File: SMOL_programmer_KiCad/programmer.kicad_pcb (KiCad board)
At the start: 2 copper layers, 9.7 x 24.9 mm, 13 parts, among them J1 Conn_02x03_Odd_Even, J2 Conn_01x05, J3 Conn_01x05

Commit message: Updated gerbs, added folder for AVR programs
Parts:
- removed REF** (x6): Mounting_Hole, samsam_footprints:Mounting_Hole
- moved R1 0.25 mm to (97.8, 111.1)
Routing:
- net /att_reset: track 7.16 -> 9.04 mm
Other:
- board size 9.7 x 24.9 mm -> 9.7 x 18.8 mm

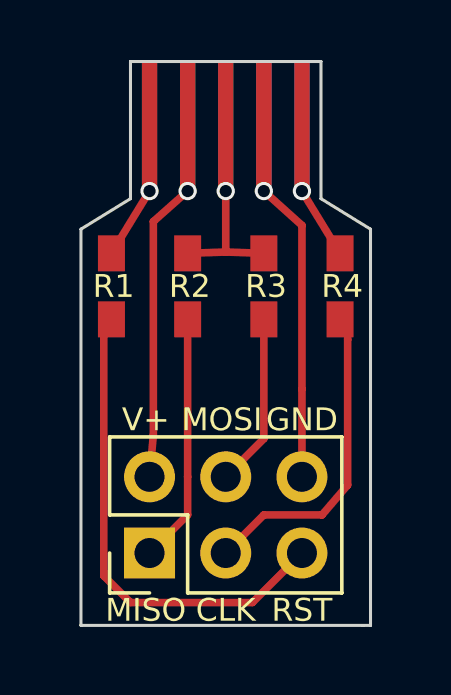
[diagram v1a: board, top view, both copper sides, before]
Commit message: re-jigging the form factor of circuit revision 6
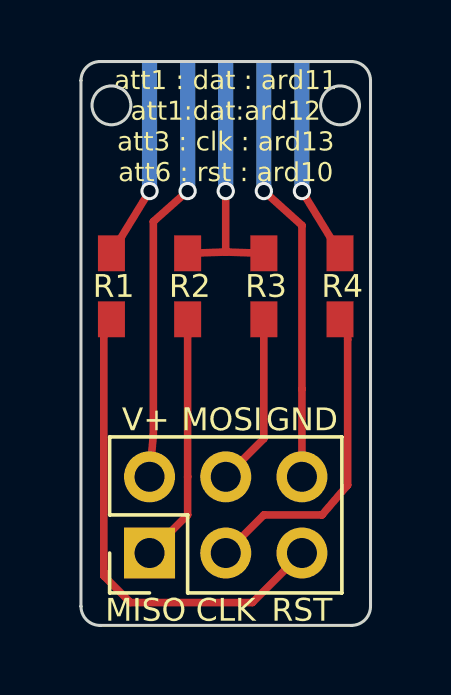
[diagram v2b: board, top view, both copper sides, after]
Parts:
- removed J2: Conn_01x05, SMOL_footprints:edgeconn
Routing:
- net /att_reset: track 9.04 -> 4.08 mm
- net GNDREF: track 15.0 -> 11.7 mm
- net /pwr: track 15.0 -> 11.7 mm
- net /att_data: track 9.53 -> 6.22 mm
- net /att_clk: track 7.39 -> 4.08 mm
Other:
- outline, holes or cut-outs redrawn
- board text added: "att1 : dat : ard11 att1:dat:ard12 att3 : clk : ard13 att6 : rst : ard10"
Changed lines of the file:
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@@
-(kicad_pcb (version 20171130) (host pcbnew "(5.0.1)-3")
+(kicad_pcb (version 20171130) (host pcbnew "(5.0.2)-1")
   (general
     (thickness 1.6)
-    (drawings 16)
-    (tracks 48)
+    (drawings 18)
+    (tracks 38)
     (zones 0)
-    (modules 7)
+    (modules 6)
     (nets 10)
   )
@@
     (36 B.SilkS user)
     (37 F.SilkS user)
-    (38 B.Mask user)
+    (38 B.Mask user hide)
     (39 F.Mask user hide)
-    (40 Dwgs.User user)
-    (41 Cmts.User user)
+    (40 Dwgs.User user hide)
+    (41 Cmts.User user hide)
     (44 Edge.Cuts user)
     (45 Margin user)
@@
     (solder_mask_min_width 0.25)
     (aux_axis_origin 0 0)
-    (visible_elements 7FEFFF7F)
+    (visible_elements 7FFFFF7F)
     (pcbplotparams
       (layerselection 0x010f0_ffffffff)
@@
     )
   )
-  (module SMOL_footprints:edgeconn (layer F.Cu)
-    (at 99.06 106.299 90)
-    (descr "Through hole straight pin header, 1x06, 2.00mm pitch, single row")
-    (tags "Through hole pin header THT 1x06 2.00mm single row")
-    (fp_text reference J2 (at 0 -2.06 90) (layer F.SilkS) hide
-      (effects (font (size 1 1) (thickness 0.15)))
-    )
-    (fp_text value Conn_01x05 (at 0.127 6.35 90) (layer F.Fab)
-      (effects (font (size 1 1) (thickness 0.15)))
-    )
-    (fp_line (start -1.5 -0.611) (end -1.5 5.658) (layer F.CrtYd) (width 0.05))
-    (fp_line (start -1.5 5.658) (end 1.5 5.658) (layer F.CrtYd) (width 0.05))
-    (fp_line (start 1.5 5.658) (end 1.5 -0.611) (layer F.CrtYd) (width 0.05))
-    (fp_line (start 1.5 -0.611) (end -1.5 -0.611) (layer F.CrtYd) (width 0.05))
-    (fp_text user %R (at 0 -2.06 90) (layer F.Fab)
-      (effects (font (size 1 1) (thickness 0.15)))
-    )
-    (pad 1 smd rect (at 0.508 0 90) (size 4.318 0.508) (layers F.Cu F.Paste F.Mask)
-      (net 6 /att_reset))
-    (pad 2 smd rect (at 0.508 1.27 90) (size 4.318 0.508) (layers F.Cu F.Paste F.Mask)
-      (net 2 /pwr))
-    (pad 3 smd rect (at 0.508 2.54 90) (size 4.318 0.508) (layers F.Cu F.Paste F.Mask)
-      (net 7 /att_data))
-    (pad 4 smd rect (at 0.508 3.81 90) (size 4.318 0.508) (layers F.Cu F.Paste F.Mask)
-      (net 8 GNDREF))
-    (pad 5 smd rect (at 0.508 5.08 90) (size 4.318 0.508) (layers F.Cu F.Paste F.Mask)
-      (net 9 /att_clk))
-    (model ${KISYS3DMOD}/Pin_Headers.3dshapes/Pin_Header_Straight_1x06_Pitch2.00mm.wrl
-      (at (xyz 0 0 0))
-      (scale (xyz 1 1 1))
-      (rotate (xyz 0 0 0))
-    )
-  )
   (module SMOL_footprints:edgeconn (layer B.Cu)
     (at 99.06 106.299 270)
@@
     )
   )
-  (gr_line (start 106.426 109.22) (end 104.775 108.204) (angle 90) (layer Edge.Cuts) (width 0.1016))
-  (gr_line (start 98.425 108.204) (end 96.774 109.22) (angle 90) (layer Edge.Cuts) (width 0.1016))
-  (gr_line (start 98.425 103.632) (end 98.425 108.204) (angle 90) (layer Edge.Cuts) (width 0.1016))
-  (gr_line (start 104.775 103.632) (end 98.425 103.632) (angle 90) (layer Edge.Cuts) (width 0.1016))
-  (gr_line (start 104.775 108.204) (end 104.775 103.632) (angle 90) (layer Edge.Cuts) (width 0.1016))
-  (gr_line (start 96.774 122.428) (end 96.774 109.22) (angle 90) (layer Edge.Cuts) (width 0.1016))
-  (gr_line (start 106.426 122.428) (end 106.426 109.22) (angle 90) (layer Edge.Cuts) (width 0.1016))
-  (gr_line (start 106.172 122.428) (end 106.426 122.428) (angle 90) (layer Edge.Cuts) (width 0.1016))
-  (gr_line (start 96.774 122.428) (end 106.172 122.428) (angle 90) (layer Edge.Cuts) (width 0.1016))
+  (gr_text "att1 : dat : ard11\natt1:dat:ard12\natt3 : clk : ard13\natt6 : rst : ard10" (at 101.6 105.791) (layer F.SilkS)
+    (effects (font (size 0.635 0.635) (thickness 0.127)))
+  )
+  (gr_arc (start 97.409 121.793) (end 96.774 121.793) (angle -90) (layer Edge.Cuts) (width 0.1016))
+  (gr_arc (start 105.791 121.793) (end 105.791 122.428) (angle -90) (layer Edge.Cuts) (width 0.1016))
+  (gr_arc (start 105.791 104.267) (end 106.426 104.267) (angle -90) (layer Edge.Cuts) (width 0.1016))
+  (gr_arc (start 97.409 104.267) (end 97.409 103.632) (angle -90) (layer Edge.Cuts) (width 0.1016))
+  (gr_circle (center 97.79 105.0925) (end 98.437575 105.0925) (layer Edge.Cuts) (width 0.1016))
+  (gr_circle (center 105.41 105.0925) (end 106.057575 105.0925) (layer Edge.Cuts) (width 0.1016))
+  (gr_line (start 105.791 103.632) (end 97.409 103.632) (angle 90) (layer Edge.Cuts) (width 0.1016))
+  (gr_line (start 96.774 121.793) (end 96.774 104.267) (angle 90) (layer Edge.Cuts) (width 0.1016))
+  (gr_line (start 106.426 121.793) (end 106.426 104.267) (angle 90) (layer Edge.Cuts) (width 0.1016))
+  (gr_line (start 97.409 122.428) (end 105.791 122.428) (angle 90) (layer Edge.Cuts) (width 0.1016))
   (gr_text GND (at 104.14 115.57) (layer F.SilkS)
     (effects (font (size 0.762 0.762) (thickness 0.1143)))
@@
   (segment (start 99.187 108.966) (end 99.187 116.078) (width 0.254) (layer F.Cu) (net 2))
   (segment (start 100.33 106.299) (end 100.33 107.95) (width 0.254) (layer B.Cu) (net 2) (status C00000))
-  (segment (start 100.33 107.95) (end 100.33 106.299) (width 0.254) (layer F.Cu) (net 2) (status C00000))
   (via (at 100.33 107.95) (size 0.6096) (drill 0.4064) (layers F.Cu B.Cu) (net 2) (status C00000))
-  (segment (start 100.33 107.95) (end 100.33 106.299) (width 0.254) (layer F.Cu) (net 2) (status C00000))
   (segment (start 101.6 120.015) (end 102.87 118.745) (width 0.254) (layer F.Cu) (net 3) (status 400000))
   (segment (start 104.811285 118.745) (end 105.664 117.750166) (width 0.254) (layer F.Cu) (net 3))
@@
   (segment (start 97.536 112.776) (end 97.79 112.224999) (width 0.254) (layer F.Cu) (net 5) (status C00000))
   (segment (start 99.06 106.299) (end 99.06 107.95) (width 0.254) (layer B.Cu) (net 6) (status C00000))
-  (segment (start 99.06 107.95) (end 99.06 106.299) (width 0.254) (layer F.Cu) (net 6) (status C00000))
   (via (at 99.06 107.95) (size 0.6096) (drill 0.4064) (layers F.Cu B.Cu) (net 6) (status C00000))
-  (segment (start 99.06 107.95) (end 99.06 106.299) (width 0.254) (layer F.Cu) (net 6) (status C00000))
   (segment (start 97.79 110.025001) (end 99.06 107.95) (width 0.254) (layer F.Cu) (net 6) (status C00000))
-  (segment (start 99.06 107.95) (end 99.06 106.299) (width 0.254) (layer F.Cu) (net 6) (status C00000))
-  (segment (start 101.6 106.299) (end 101.6 109.982) (width 0.254) (layer F.Cu) (net 7) (status 400000))
   (segment (start 101.6 109.982) (end 100.33 110.025001) (width 0.254) (layer F.Cu) (net 7) (status 800000))
   (segment (start 101.6 109.982) (end 102.87 110.025001) (width 0.254) (layer F.Cu) (net 7) (status 800000))
-  (segment (start 101.6 106.299) (end 101.6 107.95) (width 0.254) (layer F.Cu) (net 7) (status C00000))
   (segment (start 101.6 107.95) (end 101.6 106.299) (width 0.254) (layer B.Cu) (net 7) (status C00000))
   (via (at 101.6 107.95) (size 0.6096) (drill 0.4064) (layers F.Cu B.Cu) (net 7) (status C00000))
+  (segment (start 101.6 107.95) (end 101.6 109.982) (width 0.254) (layer F.Cu) (net 7))
   (segment (start 104.14 117.475) (end 104.14 114.554) (width 0.254) (layer F.Cu) (net 8) (status 400000))
   (segment (start 104.14 109.093) (end 102.87 107.95) (width 0.254) (layer F.Cu) (net 8) (status 800000))
   (segment (start 104.14 109.093) (end 104.14 114.554) (width 0.254) (layer F.Cu) (net 8))
   (segment (start 102.87 106.299) (end 102.87 107.95) (width 0.254) (layer B.Cu) (net 8) (status C00000))
-  (segment (start 102.87 107.95) (end 102.87 106.299) (width 0.254) (layer F.Cu) (net 8) (status C00000))
   (via (at 102.87 107.95) (size 0.6096) (drill 0.4064) (layers F.Cu B.Cu) (net 8) (status C00000))
-  (segment (start 102.87 107.95) (end 102.87 106.299) (width 0.254) (layer F.Cu) (net 8) (status C00000))
-  (segment (start 104.14 106.299) (end 104.14 107.95) (width 0.254) (layer F.Cu) (net 9) (status C00000))
   (segment (start 104.14 107.95) (end 104.14 106.299) (width 0.254) (layer B.Cu) (net 9) (status C00000))
   (via (at 104.14 107.95) (size 0.6096) (drill 0.4064) (layers F.Cu B.Cu) (net 9) (status C00000))
   (segment (start 105.41 110.025001) (end 104.14 107.95) (width 0.254) (layer F.Cu) (net 9) (status C00000))
-  (segment (start 104.14 107.95) (end 104.14 106.299) (width 0.254) (layer F.Cu) (net 9) (status C00000))
 )

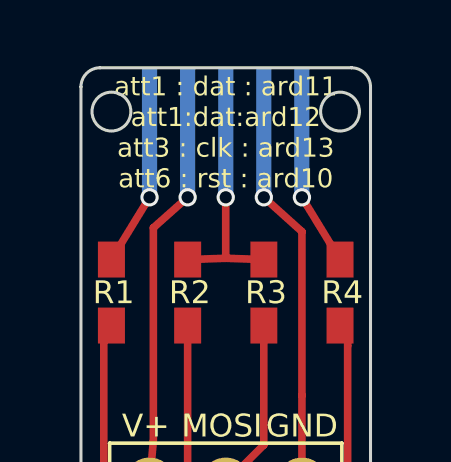
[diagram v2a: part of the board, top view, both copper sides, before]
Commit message: re-sized mounting holes to fit M1.4 bolts, like in japanese watches. Everyone has m1.4 bolts handy, right?
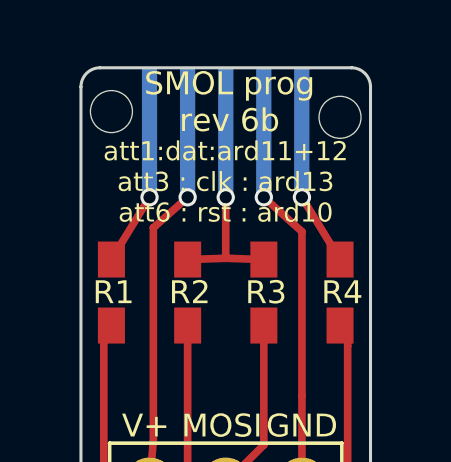
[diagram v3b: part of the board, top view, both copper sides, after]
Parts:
- added REF**: SolderWirePad_single_2mmDrill, Wire_Pads:SolderWirePad_single_2mmDrill, F.Cu at (105.4, 105.1)
- added REF**: SolderWirePad_single_2mmDrill, Wire_Pads:SolderWirePad_single_2mmDrill, F.Cu at (93.9, 104.9)
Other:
- outline, holes or cut-outs redrawn
- board text added: "SMOL prog rev 6b"
- board text added: "att1:dat:ard11+12 att3 : clk : ard13 att6 : rst : ard10"
- board text removed: "att1 : dat : ard11 att1:dat:ard12 att3 : clk : ard13 att6 : rst : ard10"
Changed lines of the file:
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@@
   (general
     (thickness 1.6)
-    (drawings 18)
+    (drawings 17)
     (tracks 38)
     (zones 0)
-    (modules 6)
+    (modules 8)
     (nets 10)
   )
@@
     (mod_text_size 1 1)
     (mod_text_width 0.15)
-    (pad_size 4.318 0.508)
-    (pad_drill 0)
+    (pad_size 1.4 1.4)
+    (pad_drill 1.4)
     (pad_to_mask_clearance 0.0508)
     (solder_mask_min_width 0.25)
@@
     (uvia_drill 0.1016)
   )
+  (module Wire_Pads:SolderWirePad_single_2mmDrill (layer F.Cu)
+    (at 105.41 105.0925)
+    (fp_text reference REF** (at 0 -3.81) (layer F.SilkS) hide
+      (effects (font (size 1 1) (thickness 0.15)))
+    )
+    (fp_text value SolderWirePad_single_2mmDrill (at -0.635 3.81) (layer F.Fab)
+      (effects (font (size 1 1) (thickness 0.15)))
+    )
+    (pad "" np_thru_hole circle (at 0 0.1905) (size 1.4 1.4) (drill 1.4) (layers *.Cu *.Mask))
+  )
   (module Pin_Headers:Pin_Header_Straight_2x03_Pitch2.54mm (layer F.Cu)
     (at 99.06 120.015 90)
@@
     )
   )
-  (gr_text "att1 : dat : ard11\natt1:dat:ard12\natt3 : clk : ard13\natt6 : rst : ard10" (at 101.6 105.791) (layer F.SilkS)
+  (module Wire_Pads:SolderWirePad_single_2mmDrill (layer F.Cu)
+    (at 93.853 104.902)
+    (fp_text reference REF** (at 0 -3.81) (layer F.SilkS) hide
+      (effects (font (size 1 1) (thickness 0.15)))
+    )
+    (fp_text value SolderWirePad_single_2mmDrill (at -0.635 3.81) (layer F.Fab)
+      (effects (font (size 1 1) (thickness 0.15)))
+    )
+    (pad "" np_thru_hole circle (at 3.937 0.1905) (size 1.4 1.4) (drill 1.4) (layers *.Cu *.Mask))
+  )
+  (gr_text "SMOL prog\nrev 6b" (at 101.727 104.775) (layer F.SilkS)
+    (effects (font (size 0.762 0.762) (thickness 0.1524)))
+  )
+  (gr_text "att1:dat:ard11+12\natt3 : clk : ard13\natt6 : rst : ard10" (at 101.6 107.442) (layer F.SilkS)
     (effects (font (size 0.635 0.635) (thickness 0.127)))
   )
@@
   (gr_arc (start 105.791 104.267) (end 106.426 104.267) (angle -90) (layer Edge.Cuts) (width 0.1016))
   (gr_arc (start 97.409 104.267) (end 97.409 103.632) (angle -90) (layer Edge.Cuts) (width 0.1016))
-  (gr_circle (center 97.79 105.0925) (end 98.437575 105.0925) (layer Edge.Cuts) (width 0.1016))
-  (gr_circle (center 105.41 105.0925) (end 106.057575 105.0925) (layer Edge.Cuts) (width 0.1016))
   (gr_line (start 105.791 103.632) (end 97.409 103.632) (angle 90) (layer Edge.Cuts) (width 0.1016))
   (gr_line (start 96.774 121.793) (end 96.774 104.267) (angle 90) (layer Edge.Cuts) (width 0.1016))

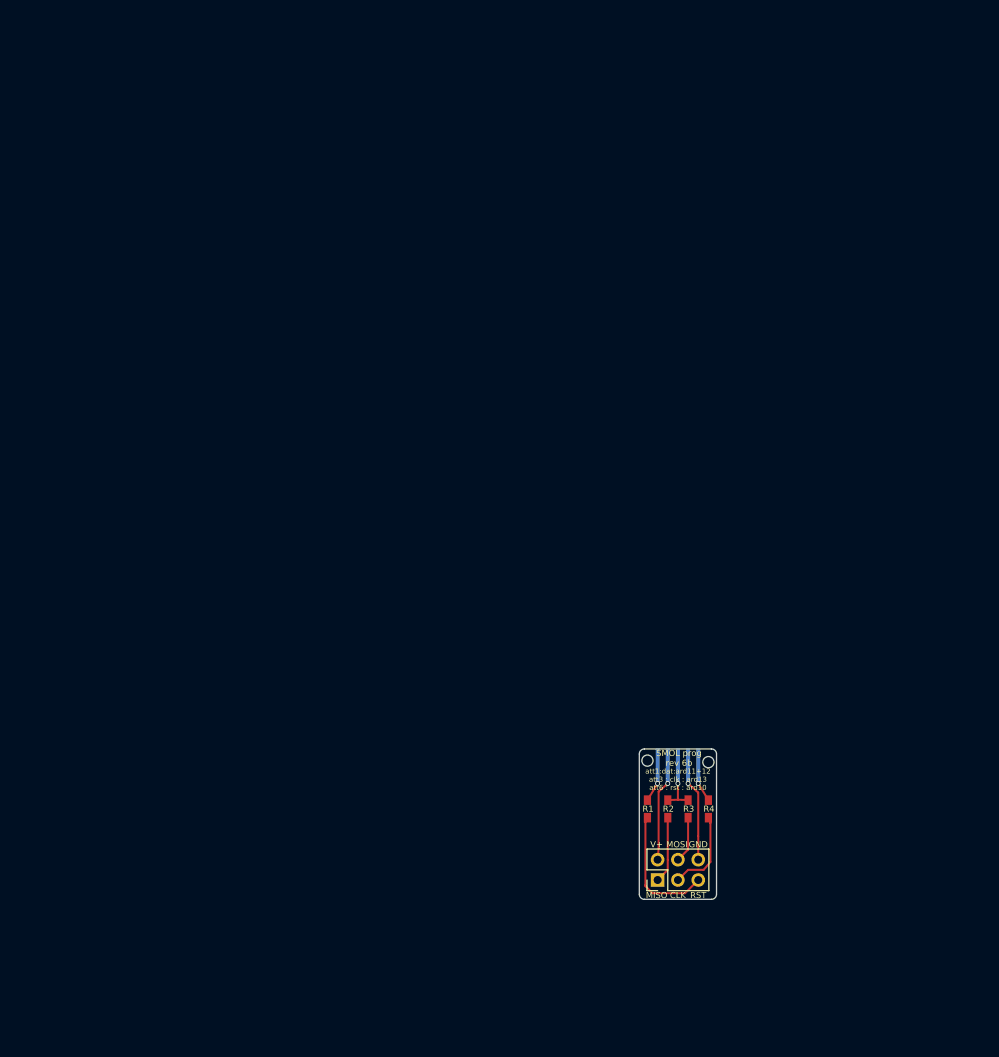
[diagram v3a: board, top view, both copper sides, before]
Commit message: overhauled programmer design; going to try pogo pins and an arduino nano shield
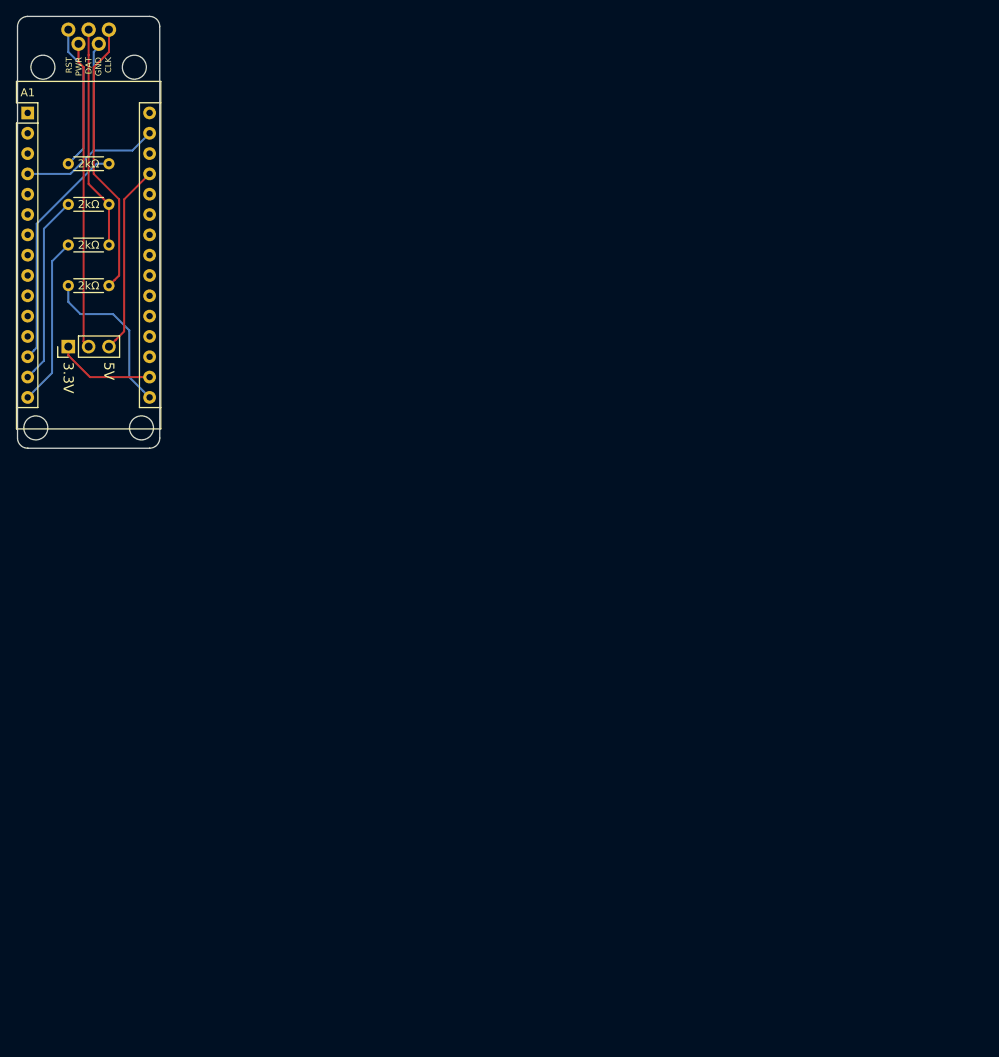
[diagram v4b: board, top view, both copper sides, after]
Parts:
- removed J3: Conn_01x05, SMOL_footprints:edgeconn
- removed R1, R2, R3, R4: 2k, SMOL_footprints:0603_HandSoldering
- removed the REF** at (105.4, 105.1)
- removed the REF** at (93.9, 104.9)
- added 2kΩ: 2k, Resistors_THT:R_Axial_DIN0204_L3.6mm_D1.6mm_P5.08mm_Horizontal, F.Cu at (30.5, 30.5)
- added 2kΩ: 2k, Resistors_THT:R_Axial_DIN0204_L3.6mm_D1.6mm_P5.08mm_Horizontal, F.Cu at (25.4, 35.6)
- added 2kΩ: 2k, Resistors_THT:R_Axial_DIN0204_L3.6mm_D1.6mm_P5.08mm_Horizontal, F.Cu at (25.4, 40.6)
- added 2kΩ: 2k, Resistors_THT:R_Axial_DIN0204_L3.6mm_D1.6mm_P5.08mm_Horizontal, F.Cu at (25.4, 45.7)
- added A1: Arduino_Nano_v3.x, Modules:Arduino_Nano, F.Cu at (20.3, 24.1)
- added J2: Conn_01x05, SMOL_footprints:edgeconn, F.Cu at (25.4, 14.6)
- added REF**: MountingHole_3.2mm_M3, Mounting_Holes:MountingHole_3.2mm_M3, F.Cu at (33.7, 18.4)
- added REF**: MountingHole_3.2mm_M3, Mounting_Holes:MountingHole_3.2mm_M3, F.Cu at (34.5, 63.5)
- added REF**: MountingHole_3.2mm_M3, Mounting_Holes:MountingHole_3.2mm_M3, F.Cu at (21.3, 63.5)
- added REF**: MountingHole_3.2mm_M3, Mounting_Holes:MountingHole_3.2mm_M3, F.Cu at (22.2, 18.4)
- J1: value Conn_02x03_Odd_Even -> Conn_01x03_Male; footprint Pin_Headers:Pin_Header_Straight_2x03_Pitch2.54mm -> Pin_Headers:Pin_Header_Straight_1x03_Pitch2.54mm
- moved J1 99.4 mm to (25.4, 53.3)
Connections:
- J1 pad 1: /prog_miso -> Net-(A1-Pad17)
- J1 pad 3: /prog_clk -> Net-(A1-Pad27)
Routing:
- net /att_clk: track 4.08 -> 34.6 mm, vias 1 -> 0
- net /pwr: track 11.7 -> 38.4 mm, vias 1 -> 0
- net Net-(A1-Pad27): track 0.00 -> 23.7 mm
- net /att_data: track 6.22 -> 28.0 mm, vias 1 -> 0
- net GNDREF: track 11.7 -> 31.6 mm, vias 1 -> 0
- net /prog_miso: track 8.32 -> 23.7 mm
- net /prog_mosi: track 5.78 -> 21.2 mm
- net /att_reset: track 4.08 -> 18.3 mm, vias 1 -> 0
- net /prog_reset: track 16.3 -> 29.2 mm
- net Net-(A1-Pad17): track 0.00 -> 12.4 mm
- net /prog_clk: track 10.6 -> 20.6 mm
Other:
- board size 9.7 x 18.8 mm -> 17.8 x 54 mm
- board text added: "3.3V"
- board text added: "5V"
- board text added: "RST PWR DAT GND CLK"
- board text removed: "CLK"
- board text removed: "GND"
- board text removed: "MISO"
- board text removed: "MOSI"
- board text removed: "RST"
- board text removed: "SMOL prog rev 6b"
- board text removed: "V+"
- board text removed: "att1 : dat : ard11 att1 : dat : ard12 att3 : clk : ard13 att6 : rst : ard10"
- board text removed: "att1:dat:ard11+12 att3 : clk : ard13 att6 : rst : ard10"
